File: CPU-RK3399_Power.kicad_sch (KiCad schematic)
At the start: 55 parts, among them U1 RK3399

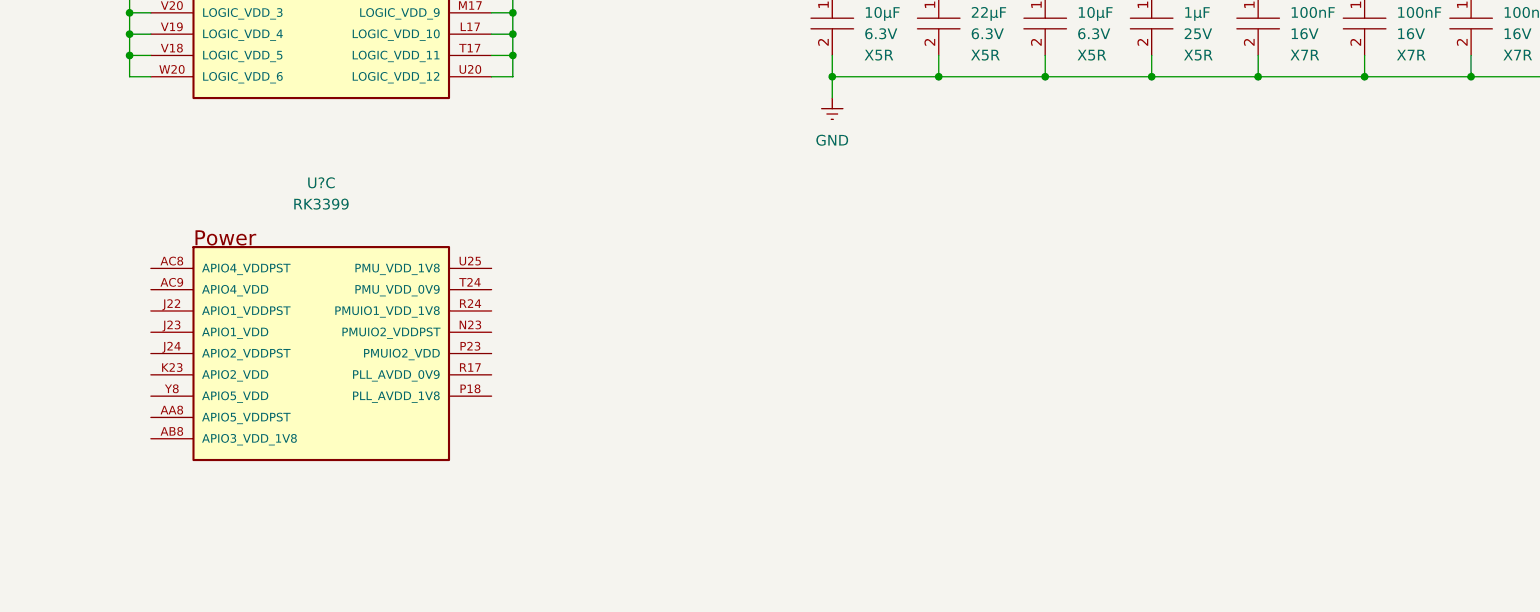
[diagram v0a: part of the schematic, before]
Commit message: update RK3399 power
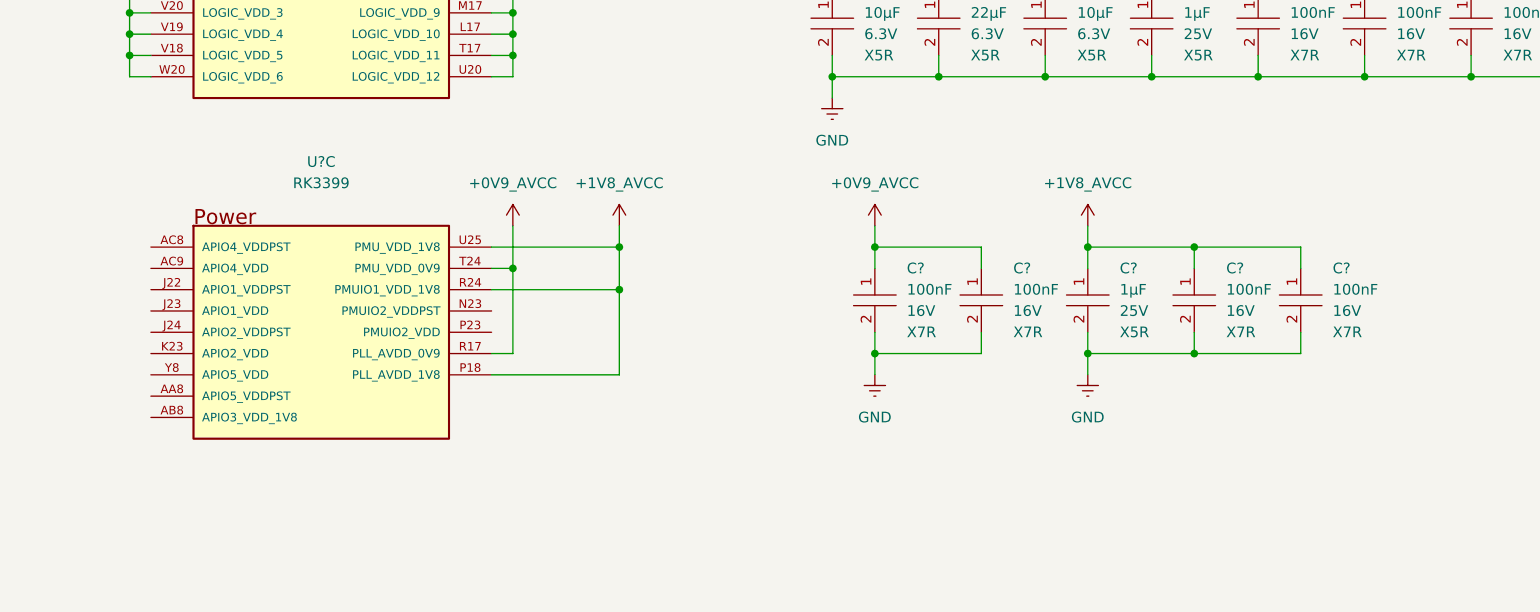
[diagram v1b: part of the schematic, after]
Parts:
- added C? (x4): ~, footprints:CAPC1005X50N, symbol component_library:Capacitors/CL05B104KO5NNNC
- added C?: ~, footprints:CAPC1005X50N, symbol component_library:Capacitors/CL05A105KA5NQNC
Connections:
- net GND: now also C?.2, C?.2, C?.2, C?.2, C?.2
- net +1V8_AVCC: now reaches U?.P18 (PLL_AVDD_1V8)
- net +1V8_AVCC: now also U?.R24 (PMUIO1_VDD_1V8), U?.U25 (PMU_VDD_1V8), C?.1, C?.1, C?.1
- net +0V9_AVCC: now reaches U?.R17 (PLL_AVDD_0V9)
- net +0V9_AVCC: now also U?.T24 (PMU_VDD_0V9), C?.1, C?.1
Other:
- moved on the sheet: U?C

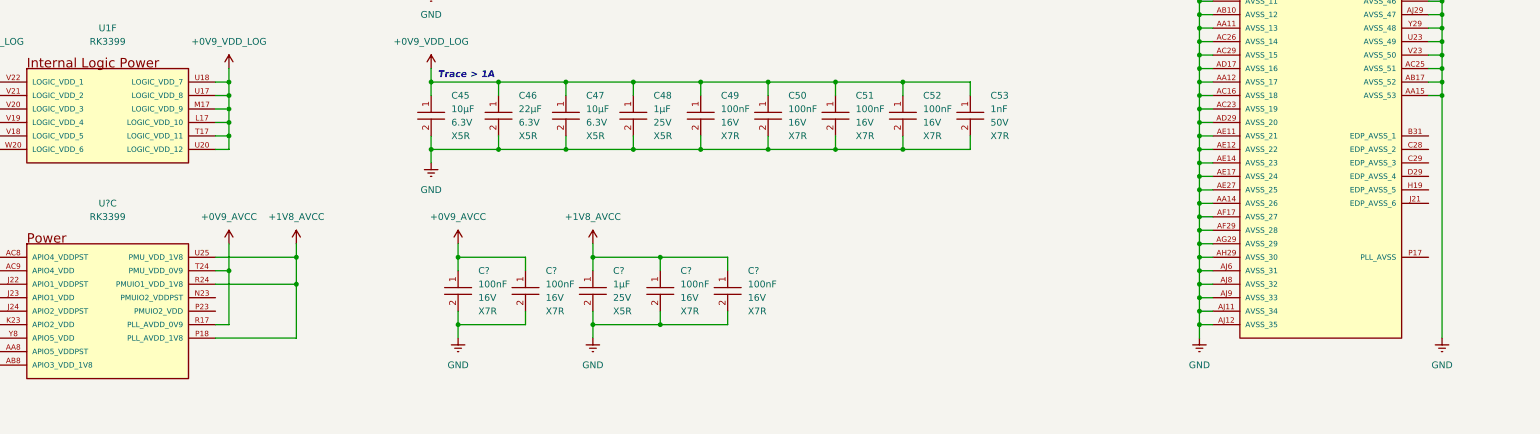
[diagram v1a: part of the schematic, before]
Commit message: design CPU DDR
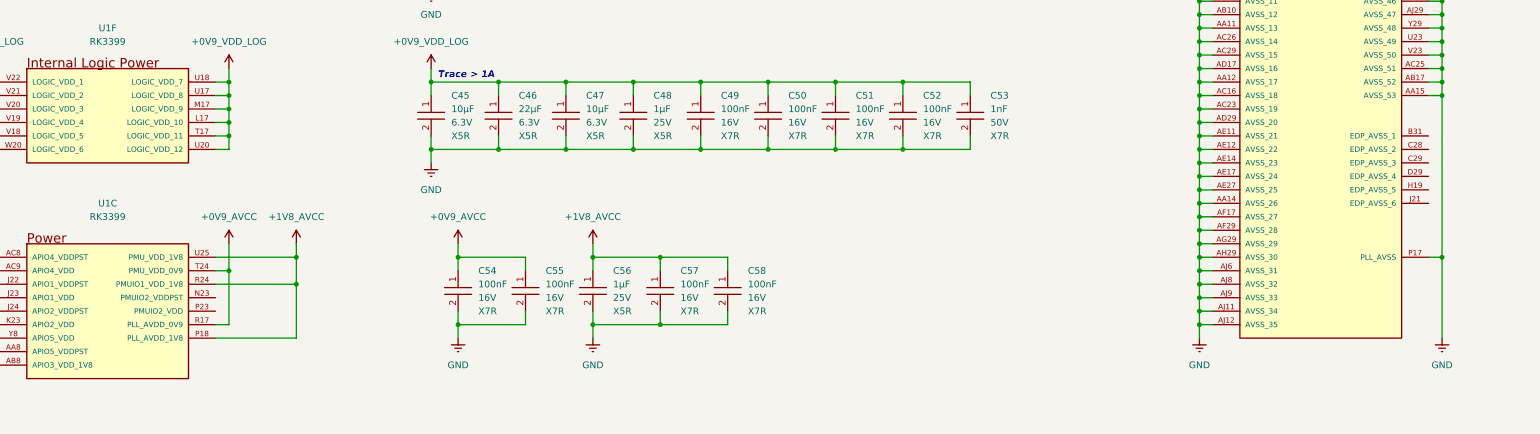
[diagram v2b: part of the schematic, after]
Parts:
- gave numbers to parts that had none: 6
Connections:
- net GND: now also U1.P17 (PLL_AVSS)
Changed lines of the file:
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@@
 	)
 	(junction
+		(at 383.54 213.36)
+		(diameter 0)
+		(color 0 0 0 0)
+	)
+	(junction
 		(at 38.1 83.82)
 		(diameter 0)
@@
 	(wire
 		(pts
+			(xy 381 213.36) (xy 383.54 213.36)
+		)
+		(stroke
+			(width 0)
+			(type default)
+		)
+	)
+	(wire
+		(pts
 			(xy 383.54 177.8) (xy 381 177.8)
 		)
@@
 	(wire
 		(pts
+			(xy 383.54 213.36) (xy 383.54 228.6)
+		)
+		(stroke
+			(width 0)
+			(type default)
+		)
+	)
+	(wire
+		(pts
 			(xy 83.82 91.44) (xy 83.82 93.98)
 		)
@@
 	(wire
 		(pts
-			(xy 383.54 182.88) (xy 383.54 228.6)
+			(xy 383.54 182.88) (xy 383.54 213.36)
 		)
 		(stroke
@@
 		(dnp no)
 		(fields_autoplaced yes)
-		(property "Reference" "#PWR023"
+		(property "Reference" "#PWR029"
 			(at 38.1 265.43 0)
 			(effects
@@
 			(project ""
 				(path "/ebc9dc57-8b05-484a-a5cd-c53b1efc71d3/a7299b18-4123-434b-8c69-0b9524fffa12/20ef5ba0-7d6c-48a6-8ce1-0c26828ee2fa"
-					(reference "#PWR023")
+					(reference "#PWR029")
 					(unit 1)
 				)
@@
 		(dnp no)
 		(fields_autoplaced yes)
-		(property "Reference" "#PWR030"
+		(property "Reference" "#PWR025"
 			(at 198.12 234.95 0)
 			(effects
@@
 			(project "VESA-SBC3399"
 				(path "/ebc9dc57-8b05-484a-a5cd-c53b1efc71d3/a7299b18-4123-434b-8c69-0b9524fffa12/20ef5ba0-7d6c-48a6-8ce1-0c26828ee2fa"
-					(reference "#PWR030")
+					(reference "#PWR025")
 					(unit 1)
 				)
@@
 		(on_board yes)
 		(dnp no)
-		(property "Reference" "C?"
+		(property "Reference" "C58"
 			(at 252.73 215.8999 0)
 			(effects
@@
 			(project "VESA-SBC3399"
 				(path "/ebc9dc57-8b05-484a-a5cd-c53b1efc71d3/a7299b18-4123-434b-8c69-0b9524fffa12/20ef5ba0-7d6c-48a6-8ce1-0c26828ee2fa"
-					(reference "C?")
+					(reference "C58")
 					(unit 1)
 				)
@@
 		(dnp no)
 		(fields_autoplaced yes)
-		(property "Reference" "#PWR027"
+		(property "Reference" "#PWR026"
 			(at 223.52 234.95 0)
 			(effects
@@
 			(project "VESA-SBC3399"
 				(path "/ebc9dc57-8b05-484a-a5cd-c53b1efc71d3/a7299b18-4123-434b-8c69-0b9524fffa12/20ef5ba0-7d6c-48a6-8ce1-0c26828ee2fa"
-					(reference "#PWR027")
+					(reference "#PWR026")
 					(unit 1)
 				)
@@
 		(on_board yes)
 		(dnp no)
-		(property "Reference" "C?"
+		(property "Reference" "C55"
 			(at 214.63 215.8999 0)
 			(effects
@@
 			(project "VESA-SBC3399"
 				(path "/ebc9dc57-8b05-484a-a5cd-c53b1efc71d3/a7299b18-4123-434b-8c69-0b9524fffa12/20ef5ba0-7d6c-48a6-8ce1-0c26828ee2fa"
-					(reference "C?")
+					(reference "C55")
 					(unit 1)
 				)
@@
 		(dnp no)
 		(fields_autoplaced yes)
-		(property "Reference" "#PWR022"
+		(property "Reference" "#PWR028"
 			(at 383.54 234.95 0)
 			(effects
@@
 			(project "VESA-SBC3399"
 				(path "/ebc9dc57-8b05-484a-a5cd-c53b1efc71d3/a7299b18-4123-434b-8c69-0b9524fffa12/20ef5ba0-7d6c-48a6-8ce1-0c26828ee2fa"
-					(reference "#PWR022")
+					(reference "#PWR028")
 					(unit 1)
 				)
@@
 		(on_board yes)
 		(dnp no)
-		(property "Reference" "#PWR026"
+		(property "Reference" "#PWR024"
 			(at 223.52 214.63 0)
 			(effects
@@
 			(project "VESA-SBC3399"
 				(path "/ebc9dc57-8b05-484a-a5cd-c53b1efc71d3/a7299b18-4123-434b-8c69-0b9524fffa12/20ef5ba0-7d6c-48a6-8ce1-0c26828ee2fa"
-					(reference "#PWR026")
+					(reference "#PWR024")
 					(unit 1)
 				)
@@
 		(on_board yes)
 		(dnp no)
-		(property "Reference" "C?"
+		(property "Reference" "C56"
 			(at 227.33 215.8999 0)
 			(effects
@@
 			(project "VESA-SBC3399"
 				(path "/ebc9dc57-8b05-484a-a5cd-c53b1efc71d3/a7299b18-4123-434b-8c69-0b9524fffa12/20ef5ba0-7d6c-48a6-8ce1-0c26828ee2fa"
-					(reference "C?")
+					(reference "C56")
 					(unit 1)
 				)
@@
 		(on_board yes)
 		(dnp no)
-		(property "Reference" "C?"
+		(property "Reference" "C54"
 			(at 201.93 215.8999 0)
 			(effects
@@
 			(project "VESA-SBC3399"
 				(path "/ebc9dc57-8b05-484a-a5cd-c53b1efc71d3/a7299b18-4123-434b-8c69-0b9524fffa12/20ef5ba0-7d6c-48a6-8ce1-0c26828ee2fa"
-					(reference "C?")
+					(reference "C54")
 					(unit 1)
 				)
@@
 		(on_board yes)
 		(dnp no)
-		(property "Reference" "#PWR028"
+		(property "Reference" "#PWR021"
 			(at 154.94 214.63 0)
 			(effects
@@
 			(project "VESA-SBC3399"
 				(path "/ebc9dc57-8b05-484a-a5cd-c53b1efc71d3/a7299b18-4123-434b-8c69-0b9524fffa12/20ef5ba0-7d6c-48a6-8ce1-0c26828ee2fa"
-					(reference "#PWR028")
+					(reference "#PWR021")
 					(unit 1)
 				)
@@
 		(on_board yes)
 		(dnp no)
-		(property "Reference" "#PWR029"
+		(property "Reference" "#PWR023"
 			(at 198.12 214.63 0)
 			(effects
@@
 			(project "VESA-SBC3399"
 				(path "/ebc9dc57-8b05-484a-a5cd-c53b1efc71d3/a7299b18-4123-434b-8c69-0b9524fffa12/20ef5ba0-7d6c-48a6-8ce1-0c26828ee2fa"
-					(reference "#PWR029")
+					(reference "#PWR023")
 					(unit 1)
 				)
@@
 		(dnp no)
 		(fields_autoplaced yes)
-		(property "Reference" "#PWR021"
+		(property "Reference" "#PWR027"
 			(at 337.82 234.95 0)
 			(effects
@@
 			(project "VESA-SBC3399"
 				(path "/ebc9dc57-8b05-484a-a5cd-c53b1efc71d3/a7299b18-4123-434b-8c69-0b9524fffa12/20ef5ba0-7d6c-48a6-8ce1-0c26828ee2fa"
-					(reference "#PWR021")
+					(reference "#PWR027")
 					(unit 1)
 				)
@@
 		(on_board yes)
 		(dnp no)
-		(property "Reference" "#PWR025"
+		(property "Reference" "#PWR022"
 			(at 167.64 214.63 0)
 			(effects
@@
 			(project "VESA-SBC3399"
 				(path "/ebc9dc57-8b05-484a-a5cd-c53b1efc71d3/a7299b18-4123-434b-8c69-0b9524fffa12/20ef5ba0-7d6c-48a6-8ce1-0c26828ee2fa"
-					(reference "#PWR025")
+					(reference "#PWR022")
 					(unit 1)
 				)
@@
 		(dnp no)
 		(fields_autoplaced yes)
-		(property "Reference" "#PWR024"
+		(property "Reference" "#PWR030"
 			(at 83.82 265.43 0)
 			(effects
@@
 			(project "VESA-SBC3399"
 				(path "/ebc9dc57-8b05-484a-a5cd-c53b1efc71d3/a7299b18-4123-434b-8c69-0b9524fffa12/20ef5ba0-7d6c-48a6-8ce1-0c26828ee2fa"
-					(reference "#PWR024")
+					(reference "#PWR030")
 					(unit 1)
 				)
@@
 		(on_board yes)
 		(dnp no)
-		(property "Reference" "C?"
+		(property "Reference" "C57"
 			(at 240.03 215.8999 0)
 			(effects
@@
 			(project "VESA-SBC3399"
 				(path "/ebc9dc57-8b05-484a-a5cd-c53b1efc71d3/a7299b18-4123-434b-8c69-0b9524fffa12/20ef5ba0-7d6c-48a6-8ce1-0c26828ee2fa"
-					(reference "C?")
+					(reference "C57")
 					(unit 1)
 				)
@@
 		(dnp no)
 		(fields_autoplaced yes)
-		(property "Reference" "U?"
+		(property "Reference" "U1"
 			(at 132.08 203.2 0)
 			(effects
@@
 			(project ""
 				(path "/ebc9dc57-8b05-484a-a5cd-c53b1efc71d3/a7299b18-4123-434b-8c69-0b9524fffa12/20ef5ba0-7d6c-48a6-8ce1-0c26828ee2fa"
-					(reference "U?")
+					(reference "U1")
 					(unit 29)
 				)

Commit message: design CPU-RK3399 eMMC Controller
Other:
- company: (none) -> TickLab
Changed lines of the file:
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@@
 	(title_block
 		(title "CPU-RK3399 Power")
-		(date "2026-01-09")
+		(date "2026-01-14")
 		(rev "1.0.0")
+		(company "TickLab")
 	)
 	(text "The high-capacity capacitors should be placed\nclose to CPU power pins, on the opposite"

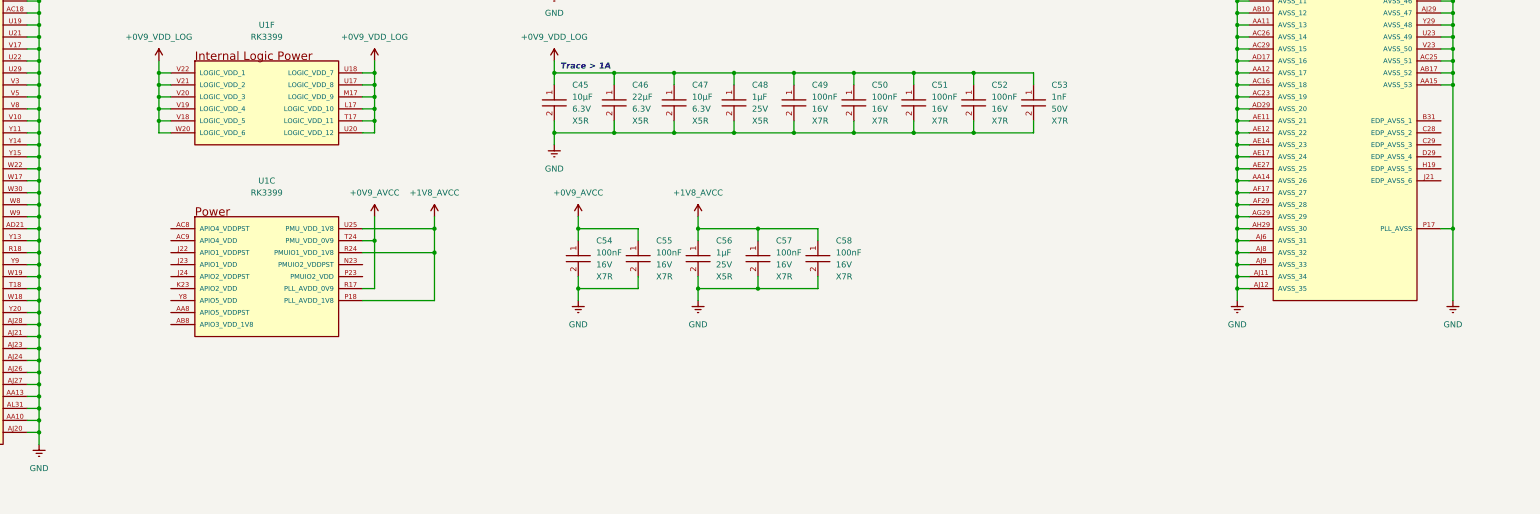
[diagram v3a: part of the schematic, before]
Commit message: update schematic
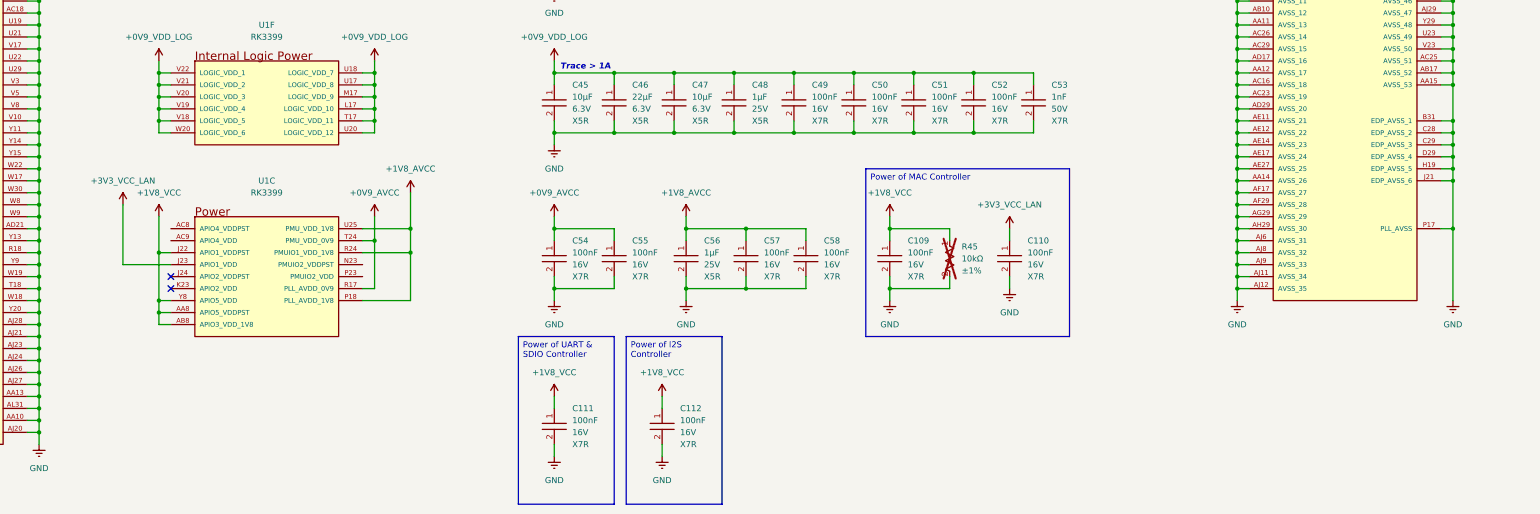
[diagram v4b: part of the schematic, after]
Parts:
- added C109, C110, C111, C112: ~, footprints:CAPC1005X50N, symbol component_library:Capacitors/CL05B104KO5NNNC
- added R45: ~, footprints:RESC1005X35N, symbol component_library:Resistors/0402WGF1002TCE
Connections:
- net GND: now also U1.B31 (EDP_AVSS_1), U1.C28 (EDP_AVSS_2), U1.C29 (EDP_AVSS_3), U1.D29 (EDP_AVSS_4), U1.H19 (EDP_AVSS_5), U1.J21 (EDP_AVSS_6), C109.2, C110.2, C111.2, C112.2, R45.2
- net +1V8_VCC: now reaches U1.AA8 (APIO5_VDDPST)
- net +1V8_VCC: now also U1.AB8 (APIO3_VDD_1V8), U1.J22 (APIO1_VDDPST), U1.Y8 (APIO5_VDD), C109.1, C111.1, C112.1, R45.1
- net +3V3_VCC_LAN: now reaches U1.J23 (APIO1_VDD)
- net +3V3_VCC_LAN: now also C110.1
- no-connect marks 0 -> 2
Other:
- moved on the sheet: C54, C55, C56, C57, C58

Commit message: design PMIC
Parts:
- added C113, C114, C115: ~, footprints:CAPC1005X50N, symbol component_library:Capacitors/CL05B104KO5NNNC
- added R64: ~, footprints:RESC1005X35N, symbol component_library:Resistors/0402WGF1002TCE
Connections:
- net +1V8_VCC: now also U1.N23 (PMUIO2_VDDPST), U1.P23 (PMUIO2_VDD), C113.1
- net GND: now also C113.2, C114.2, C115.2, R64.2
- net +1V5_VCC: now reaches U1.AC8 (APIO4_VDDPST)
- net +1V5_VCC: now also C115.1, R64.1
- net +3V0_VCC: now reaches U1.AC9 (APIO4_VDD)
- net +3V0_VCC: now also C114.1
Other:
- moved on the sheet: C1, C10, C109, C11, C110, C111, C112, C12, C13, C14, C15, C16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

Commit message: update design power
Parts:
- renumbered C54 to C100, C55 to C101, C56 to C102, C57 to C103, C58 to C104, C109 to C105, C110 to C106, C111 to C107, C112 to C108, C113 to C109, C114 to C110, C115 to C111, C1 to C47, C2 to C48, C3 to C49, C4 to C50, C5 to C51, C6 to C52, C7 to C53, C8 to C54, C9 to C55, C10 to C56, C11 to C57, C12 to C58, C13 to C59, C14 to C60, C15 to C61, C16 to C62, C17 to C63, C18 to C64, C19 to C65, C20 to C66, C21 to C67, C22 to C68, C23 to C69, C24 to C70, C25 to C71, C26 to C72, C27 to C73, C28 to C74, C29 to C75, C30 to C76, C31 to C77, C32 to C78, C33 to C79, C34 to C80, C35 to C81, C36 to C82, C37 to C83, C38 to C84, C39 to C85, C40 to C86, C41 to C87, C42 to C88, C43 to C89, C44 to C90, C45 to C91, C46 to C92, C47 to C93, C48 to C94, C49 to C95, C50 to C96, C51 to C97, C52 to C98, C53 to C99, R45 to R15, R64 to R16, U1 to U2

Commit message: design DDR
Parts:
- renumbered C47 to C174, C48 to C175, C49 to C176, C50 to C177, C51 to C178, C52 to C179, C53 to C180, C54 to C181, C55 to C182, C56 to C183, C57 to C184, C58 to C185, C59 to C186, C60 to C187, C61 to C188, C62 to C189, C63 to C190, C64 to C191, C65 to C192, C66 to C193, C67 to C194, C68 to C195, C69 to C196, C70 to C197, C71 to C198, C72 to C199, C73 to C200, C74 to C201, C75 to C202, C76 to C203, C77 to C204, C78 to C205, C79 to C206, C80 to C207, C81 to C208, C82 to C209, C83 to C210, C84 to C211, C85 to C212, C86 to C213, C87 to C214, C88 to C215, C89 to C216, C90 to C217, C91 to C218, C92 to C219, C93 to C220, C94 to C221, C95 to C222, C96 to C223, C97 to C224, C98 to C225, C99 to C226, C100 to C227, C101 to C228, C102 to C229, C103 to C230, C104 to C231, C105 to C232, C106 to C233, C107 to C234, C108 to C235, C109 to C236, C110 to C237, C111 to C238, R15 to R86, R16 to R87, U2 to U17
